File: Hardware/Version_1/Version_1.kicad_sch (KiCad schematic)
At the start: 94 parts, among them IC1 LIFCL-40-7BG256C, IC2 W25R256JVEIQ, IC3 IS46TR16128D-125KBLA2, IC4 TPS62A01DRLR, IC5 TPS62A01DRLR, IC6 TPS62A01DRLR, J1 GPIO, J2 Conn_01x05_Pin, J3 52435-2271, J4 52435-2271, U1 CAT24C256, Y1 AK3ADDF1-156.2500T3

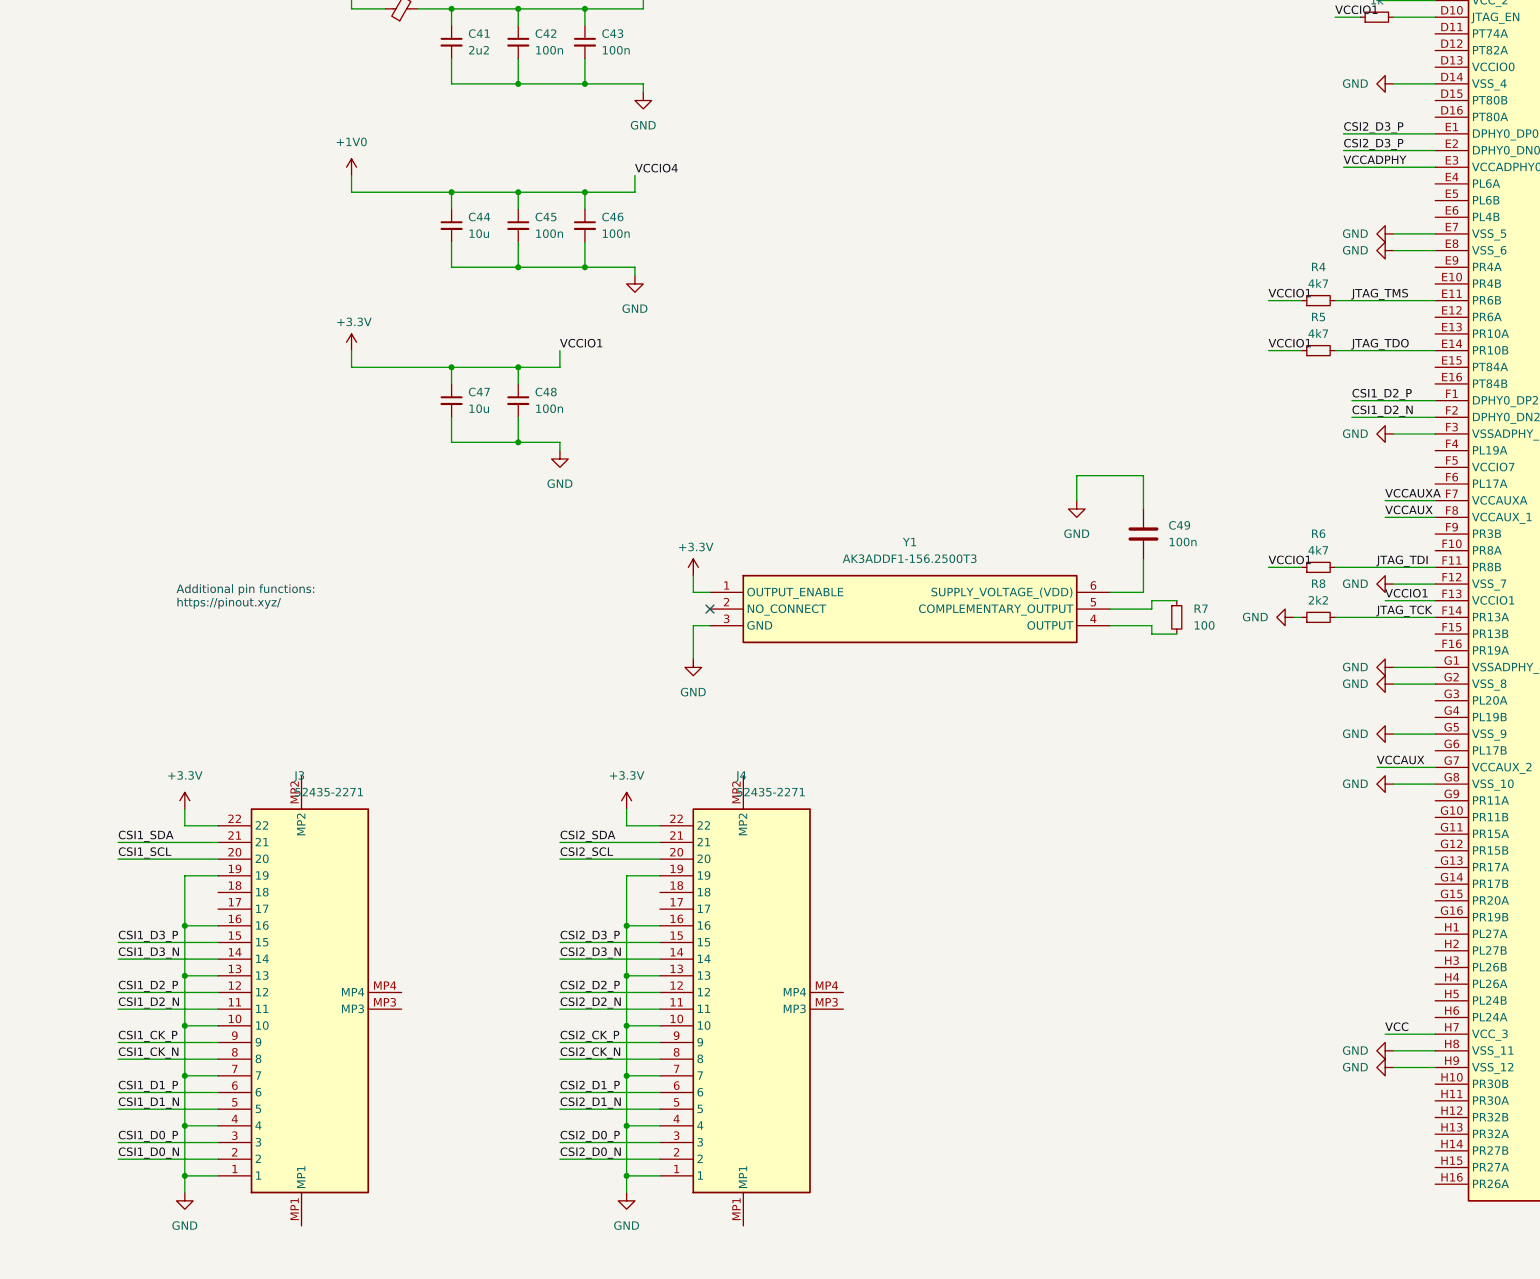
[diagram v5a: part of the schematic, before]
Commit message: mipi routing
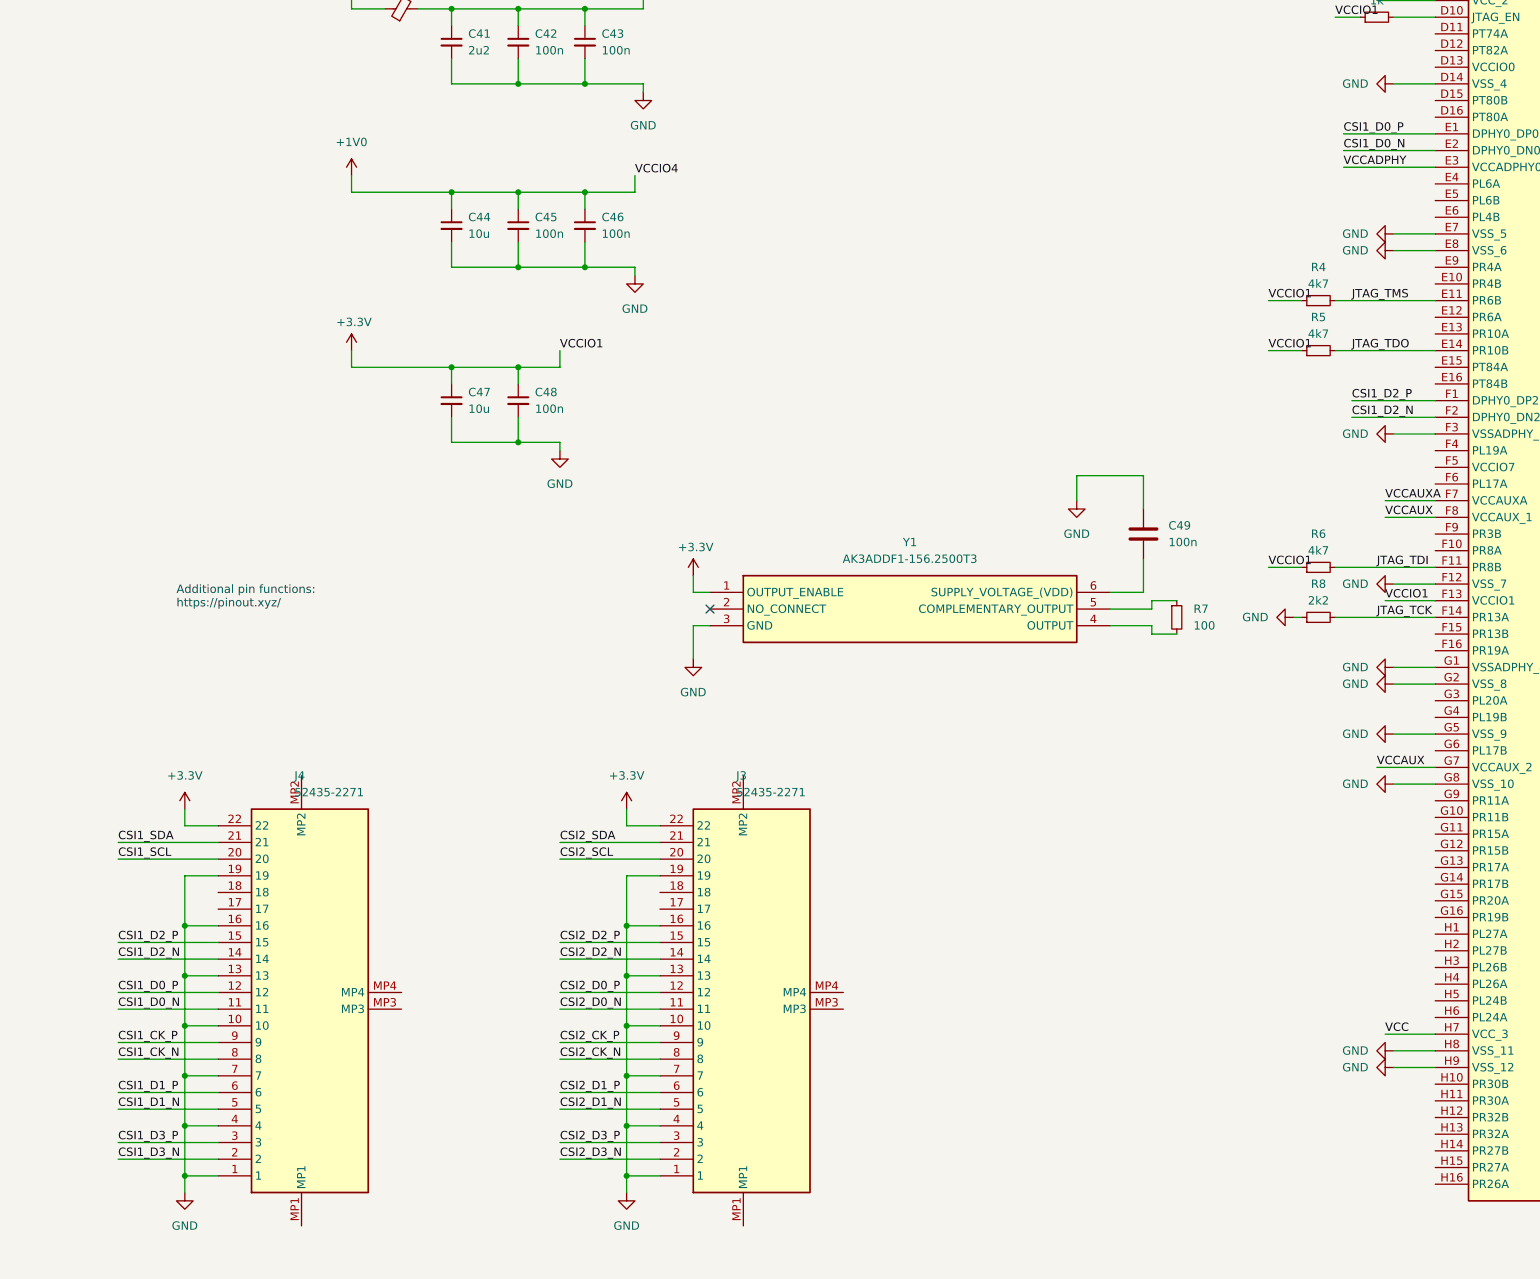
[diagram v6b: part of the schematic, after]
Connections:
- net CSI1_CK_N: now also J4.8; no longer J3.8
- net CSI1_CK_P: now also J4.9; no longer J3.9
- net CSI1_D0_N: now also IC1.E2 (DPHY0_DN0), J4.11; no longer J3.2
- net CSI1_D0_P: now also IC1.E1 (DPHY0_DP0), J4.12; no longer J3.3
- net CSI1_D1_N: now also J4.5; no longer J3.5
- net CSI1_D1_P: now also J4.6; no longer J3.6
- net CSI1_D2_N: now also J4.14; no longer J3.11
- net CSI1_D2_P: now also J4.15; no longer J3.12
- net CSI1_D3_N: now also J4.2; no longer J3.14
- net CSI1_D3_P: now also J4.3; no longer J3.15
- net CSI1_SCL: now also J4.20; no longer J3.20
- net CSI1_SDA: now also J4.21; no longer J3.21
- net CSI2_CK_N: now also J3.8; no longer J4.8
- net CSI2_CK_P: now also J3.9; no longer J4.9
- net CSI2_D0_N: now also J3.11; no longer J4.2
- net CSI2_D0_P: now also J3.12; no longer J4.3
- net CSI2_D1_N: now also J3.5; no longer J4.5
- net CSI2_D1_P: now also J3.6; no longer J4.6
- net CSI2_D2_N: now also J3.14; no longer J4.11
- net CSI2_D2_P: now also J3.15; no longer J4.12
- net CSI2_D3_N: now also J3.2; no longer J4.14
- net CSI2_D3_P: now also J3.3; no longer IC1.E1 (DPHY0_DP0), IC1.E2 (DPHY0_DN0), J4.15
- net CSI2_SCL: now also J3.20; no longer J4.20
- net CSI2_SDA: now also J3.21; no longer J4.21
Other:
- moved on the sheet: J3, J4
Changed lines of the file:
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@@
     (effects (font (size 1.27 1.27)) (justify left bottom))
   )
-  (label "CSI2_D0_P" (at 222.25 367.03 0) (fields_autoplaced)
+  (label "CSI2_D3_P" (at 222.25 367.03 0) (fields_autoplaced)
     (effects (font (size 1.27 1.27)) (justify left bottom))
   )
@@
     (effects (font (size 1.27 1.27)) (justify left bottom))
   )
-  (label "CSI2_D3_N" (at 222.25 339.09 0) (fields_autoplaced)
+  (label "CSI2_D2_N" (at 222.25 339.09 0) (fields_autoplaced)
     (effects (font (size 1.27 1.27)) (justify left bottom))
   )
@@
     (effects (font (size 1.27 1.27)) (justify left bottom))
   )
-  (label "CSI2_D2_N" (at 222.25 346.71 0) (fields_autoplaced)
+  (label "CSI2_D0_N" (at 222.25 346.71 0) (fields_autoplaced)
     (effects (font (size 1.27 1.27)) (justify left bottom))
   )
@@
     (effects (font (size 1.27 1.27)) (justify left bottom))
   )
-  (label "CSI2_D3_P" (at 341.63 213.36 0) (fields_autoplaced)
+  (label "CSI1_D0_P" (at 341.63 213.36 0) (fields_autoplaced)
     (effects (font (size 1.27 1.27)) (justify left bottom))
   )
@@
     (effects (font (size 1.27 1.27)) (justify left bottom))
   )
-  (label "CSI2_D0_N" (at 222.25 369.57 0) (fields_autoplaced)
+  (label "CSI2_D3_N" (at 222.25 369.57 0) (fields_autoplaced)
     (effects (font (size 1.27 1.27)) (justify left bottom))
   )
@@
     (effects (font (size 1.27 1.27)) (justify left bottom))
   )
-  (label "CSI1_D2_P" (at 154.94 344.17 0) (fields_autoplaced)
+  (label "CSI1_D0_P" (at 154.94 344.17 0) (fields_autoplaced)
     (effects (font (size 1.27 1.27)) (justify left bottom))
   )
@@
     (effects (font (size 1.27 1.27)) (justify left bottom))
   )
-  (label "CSI1_D0_N" (at 154.94 369.57 0) (fields_autoplaced)
+  (label "CSI1_D3_N" (at 154.94 369.57 0) (fields_autoplaced)
     (effects (font (size 1.27 1.27)) (justify left bottom))
   )
@@
     (effects (font (size 1.27 1.27)) (justify left bottom))
   )
-  (label "CSI1_D2_N" (at 154.94 346.71 0) (fields_autoplaced)
+  (label "CSI1_D0_N" (at 154.94 346.71 0) (fields_autoplaced)
     (effects (font (size 1.27 1.27)) (justify left bottom))
   )
@@
     (effects (font (size 1.27 1.27)) (justify right bottom))
   )
-  (label "CSI1_D3_P" (at 154.94 336.55 0) (fields_autoplaced)
+  (label "CSI1_D2_P" (at 154.94 336.55 0) (fields_autoplaced)
     (effects (font (size 1.27 1.27)) (justify left bottom))
   )
@@
     (effects (font (size 1.27 1.27)) (justify left bottom))
   )
-  (label "CSI2_D2_P" (at 222.25 344.17 0) (fields_autoplaced)
+  (label "CSI2_D0_P" (at 222.25 344.17 0) (fields_autoplaced)
     (effects (font (size 1.27 1.27)) (justify left bottom))
   )
@@
     (effects (font (size 1.27 1.27)) (justify left bottom))
   )
-  (label "CSI2_D3_P" (at 341.63 215.9 0) (fields_autoplaced)
+  (label "CSI1_D0_N" (at 341.63 215.9 0) (fields_autoplaced)
     (effects (font (size 1.27 1.27)) (justify left bottom))
   )
@@
     (effects (font (size 1.27 1.27)) (justify left bottom))
   )
-  (label "CSI1_D0_P" (at 154.94 367.03 0) (fields_autoplaced)
+  (label "CSI1_D3_P" (at 154.94 367.03 0) (fields_autoplaced)
     (effects (font (size 1.27 1.27)) (justify left bottom))
   )
@@
     (effects (font (size 1.27 1.27)) (justify left bottom))
   )
-  (label "CSI2_D3_P" (at 222.25 336.55 0) (fields_autoplaced)
+  (label "CSI2_D2_P" (at 222.25 336.55 0) (fields_autoplaced)
     (effects (font (size 1.27 1.27)) (justify left bottom))
   )
-  (label "CSI1_D3_N" (at 154.94 339.09 0) (fields_autoplaced)
+  (label "CSI1_D2_N" (at 154.94 339.09 0) (fields_autoplaced)
     (effects (font (size 1.27 1.27)) (justify left bottom))
   )
@@
     )
   )
-  (symbol (lib_id "Component:52435-2271") (at 250.19 379.73 90) (unit 1)
+  (symbol (lib_id "Component:52435-2271") (at 182.88 379.73 90) (unit 1)
     (in_bom yes) (on_board yes) (dnp no) (fields_autoplaced)
-    (property "Reference" "J4" (at 249.1039 311.15 90)
+    (property "Reference" "J4" (at 181.7939 311.15 90)
       (effects (font (size 1.27 1.27)) (justify right))
     )
-    (property "Value" "52435-2271" (at 249.1039 313.69 90)
+    (property "Value" "52435-2271" (at 181.7939 313.69 90)
       (effects (font (size 1.27 1.27)) (justify right))
     )
-    (property "Footprint" "524352271" (at 340.03 314.96 0)
+    (property "Footprint" "524352271" (at 272.72 314.96 0)
       (effects (font (size 1.27 1.27)) (justify left top) hide)
     )
-    (property "Datasheet" "https://www.molex.com/pdm_docs/sd/524352271_sd.pdf" (at 440.03 314.96 0)
+    (property "Datasheet" "https://www.molex.com/pdm_docs/sd/524352271_sd.pdf" (at 372.72 314.96 0)
       (effects (font (size 1.27 1.27)) (justify left top) hide)
     )
-    (property "Height" "2.2" (at 640.03 314.96 0)
+    (property "Height" "2.2" (at 572.72 314.96 0)
       (effects (font (size 1.27 1.27)) (justify left top) hide)
     )
-    (property "Manufacturer_Name" "Molex" (at 740.03 314.96 0)
+    (property "Manufacturer_Name" "Molex" (at 672.72 314.96 0)
       (effects (font (size 1.27 1.27)) (justify left top) hide)
     )
-    (property "Manufacturer_Part_Number" "52435-2271" (at 840.03 314.96 0)
+    (property "Manufacturer_Part_Number" "52435-2271" (at 772.72 314.96 0)
       (effects (font (size 1.27 1.27)) (justify left top) hide)
     )
-    (property "Mouser Part Number" "538-52435-2271" (at 940.03 314.96 0)
+    (property "Mouser Part Number" "538-52435-2271" (at 872.72 314.96 0)
       (effects (font (size 1.27 1.27)) (justify left top) hide)
     )
-    (property "Mouser Price/Stock" "https://www.mouser.co.uk/ProductDetail/Molex/52435-2271?qs=R7%2FZKp6KZ2YF65bXSszUKA%3D%3D" (at 1040.03 314.96 0)
+    (property "Mouser Price/Stock" "https://www.mouser.co.uk/ProductDetail/Molex/52435-2271?qs=R7%2FZKp6KZ2YF65bXSszUKA%3D%3D" (at 972.72 314.96 0)
       (effects (font (size 1.27 1.27)) (justify left top) hide)
     )
-    (property "Arrow Part Number" "" (at 1140.03 314.96 0)
+    (property "Arrow Part Number" "" (at 1072.72 314.96 0)
       (effects (font (size 1.27 1.27)) (justify left top) hide)
     )
-    (property "Arrow Price/Stock" "" (at 1240.03 314.96 0)
+    (property "Arrow Price/Stock" "" (at 1172.72 314.96 0)
       (effects (font (size 1.27 1.27)) (justify left top) hide)
     )
@@
     )
   )
-  (symbol (lib_id "Component:52435-2271") (at 182.88 379.73 90) (unit 1)
+  (symbol (lib_id "Component:52435-2271") (at 250.19 379.73 90) (unit 1)
     (in_bom yes) (on_board yes) (dnp no) (fields_autoplaced)
-    (property "Reference" "J3" (at 181.7939 311.15 90)
+    (property "Reference" "J3" (at 249.1039 311.15 90)
       (effects (font (size 1.27 1.27)) (justify right))
     )
-    (property "Value" "52435-2271" (at 181.7939 313.69 90)
+    (property "Value" "52435-2271" (at 249.1039 313.69 90)
       (effects (font (size 1.27 1.27)) (justify right))
     )
-    (property "Footprint" "524352271" (at 272.72 314.96 0)
+    (property "Footprint" "524352271" (at 340.03 314.96 0)
       (effects (font (size 1.27 1.27)) (justify left top) hide)
     )
-    (property "Datasheet" "https://www.molex.com/pdm_docs/sd/524352271_sd.pdf" (at 372.72 314.96 0)
+    (property "Datasheet" "https://www.molex.com/pdm_docs/sd/524352271_sd.pdf" (at 440.03 314.96 0)
       (effects (font (size 1.27 1.27)) (justify left top) hide)
     )
-    (property "Height" "2.2" (at 572.72 314.96 0)
+    (property "Height" "2.2" (at 640.03 314.96 0)
       (effects (font (size 1.27 1.27)) (justify left top) hide)
     )
-    (property "Manufacturer_Name" "Molex" (at 672.72 314.96 0)
+    (property "Manufacturer_Name" "Molex" (at 740.03 314.96 0)
       (effects (font (size 1.27 1.27)) (justify left top) hide)
     )
-    (property "Manufacturer_Part_Number" "52435-2271" (at 772.72 314.96 0)
+    (property "Manufacturer_Part_Number" "52435-2271" (at 840.03 314.96 0)
       (effects (font (size 1.27 1.27)) (justify left top) hide)
     )
-    (property "Mouser Part Number" "538-52435-2271" (at 872.72 314.96 0)
+    (property "Mouser Part Number" "538-52435-2271" (at 940.03 314.96 0)
       (effects (font (size 1.27 1.27)) (justify left top) hide)
     )
-    (property "Mouser Price/Stock" "https://www.mouser.co.uk/ProductDetail/Molex/52435-2271?qs=R7%2FZKp6KZ2YF65bXSszUKA%3D%3D" (at 972.72 314.96 0)
+    (property "Mouser Price/Stock" "https://www.mouser.co.uk/ProductDetail/Molex/52435-2271?qs=R7%2FZKp6KZ2YF65bXSszUKA%3D%3D" (at 1040.03 314.96 0)
       (effects (font (size 1.27 1.27)) (justify left top) hide)
     )
-    (property "Arrow Part Number" "" (at 1072.72 314.96 0)
+    (property "Arrow Part Number" "" (at 1140.03 314.96 0)
       (effects (font (size 1.27 1.27)) (justify left top) hide)
     )
-    (property "Arrow Price/Stock" "" (at 1172.72 314.96 0)
+    (property "Arrow Price/Stock" "" (at 1240.03 314.96 0)
       (effects (font (size 1.27 1.27)) (justify left top) hide)
     )

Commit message: Added i2c and flash chip
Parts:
- removed J1: GPIO, Connector_PinSocket_2.54mm:PinSocket_2x20_P2.54mm_Vertical, symbol Connector_Generic:Conn_02x20_Odd_Even
- added DONE1, INITN1: TestPoint, TestPoint:TestPoint_Pad_D1.0mm, symbol Connector:TestPoint
- added J6: GPIO, Connector_PinSocket_2.54mm:PinSocket_2x20_P2.54mm_Vertical, symbol Connector_Generic:Conn_02x20_Odd_Even
- added R18: 1k0, Resistor_SMD:R_0603_1608Metric, symbol Device:R_Small
- added R19, R20: 4k7, Resistor_SMD:R_0603_1608Metric, symbol Device:R_Small
- added R21, R22: 10k0, Resistor_SMD:R_0402_1005Metric, symbol Device:R_Small
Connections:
- net +3.3V: now also R19.1, R20.1
- net +3V3: now also C49.1, Y1.6 (SUPPLY_VOLTAGE_(VDD)), J6.1 (+3V3), J6.17 (+3V3)
- net +5V: now also J6.2 (+5V), J6.4 (+5V)
- net CSI1_SCL: now also IC1.G13 (PR17A)
- net CSI1_SDA: now also IC1.G14 (PR17B)
- net CSI2_SCL: now also IC1.G16 (PR19B)
- net CSI2_SDA: now also IC1.F16 (PR19A)
- net GND: now also C49.2, J6.14 (GND), J6.20 (GND), J6.25 (GND), J6.30 (GND), J6.34 (GND), J6.39 (GND), J6.6 (GND), J6.9 (GND), R18.2, R22.2; no longer C49.1
- net GPIO10/SPI0.MOSI: now also J6.19 (GPIO10/SPI0.MOSI)
- net GPIO11/SPI0.SCLK: now also J6.23 (GPIO11/SPI0.SCLK)
- net GPIO12/PWM0: now also J6.32 (GPIO12/PWM0)
- net GPIO13/PWM1: now also J6.33 (GPIO13/PWM1)
- net GPIO14/TXD0: now also J6.8 (GPIO14/TXD0)
- net GPIO15/RXD0: now also J6.10 (GPIO15/RXD0)
- net GPIO16: now also J6.36 (GPIO16)
- net GPIO17: now also J6.11 (GPIO17)
- net GPIO18/PCM.CLK: now also J6.12 (GPIO18/PCM.CLK)
- net GPIO19/PCM.FS: now also J6.35 (GPIO19/PCM.FS)
- net GPIO20/PCM.DIN: now also J6.38 (GPIO20/PCM.DIN)
- net GPIO21/PCM.DOUT: now also J6.40 (GPIO21/PCM.DOUT)
- net GPIO22: now also J6.15 (GPIO22)
- net GPIO23: now also J6.16 (GPIO23)
- net GPIO24: now also J6.18 (GPIO24)
- net GPIO25: now also J6.22 (GPIO25)
- net GPIO26: now also J6.37 (GPIO26)
- net GPIO27: now also J6.13 (GPIO27)
- net GPIO5: now also J6.29 (GPIO5)
- net GPIO6: now also J6.31 (GPIO6)
- net GPIO7/SPI0.CE1: now also J6.26 (GPIO7/SPI0.CE1)
- net GPIO8/SPI0.CE0: now also J6.24 (GPIO8/SPI0.CE0)
- net GPIO9/SPI0.MISO: now also J6.21 (GPIO9/SPI0.MISO)
- net ID_SCL: now also J6.28 (ID_SCL)
- net ID_SDA: now also J6.27 (ID_SDA)
- net VCCDRAM: now also IC3.T2 (RESET#), R21.1
- net DONE: now reaches IC1.B16 (PT76B)
- net DONE: now also DONE1.1
- net PROGRAMN: now reaches IC1.C12 (PT74B)
- net PROGRAMN: now also J6.7 (GPIO4/GPCLK0), R20.2
- net MD0: now reaches IC1.C14 (PT78B)
- net MD0: now also IC2.5 (IO0)
- net MCSN: now reaches IC1.C15 (PT78A)
- net MCSN: now also IC2.1 (~{CS}), R19.2
- net MCLK: now reaches IC1.C16 (PT76A)
- net MCLK: now also IC2.6 (CLK), R18.1
- net INITN: now reaches IC1.D11 (PT74A)
- net INITN: now also INITN1.1
- net MD3: now reaches IC1.D12 (PT82A)
- net MD3: now also IC2.7 (IO3)
- net MD2: now reaches IC1.D15 (PT80B)
- net MD2: now also IC2.3 (IO2)
- net MD1: now reaches IC1.D16 (PT80A)
- net MD1: now also IC2.2 (IO1)
- net SLAVE_I2C_SCL: now reaches IC1.G10 (PR11B)
- net SLAVE_I2C_SCL: now also J6.5 (GPIO3/SCL1)
- net SLAVE_I2C_SDA: now reaches IC1.G9 (PR11A)
- net SLAVE_I2C_SDA: now also J6.3 (GPIO2/SDA1)
- net REFCLK_N: now reaches IC1.M4 (PB6B)
- net REFCLK_N: now also R7.1, Y1.5 (COMPLEMENTARY_OUTPUT)
- net REFCLK_P: now reaches IC1.N4 (PB6A)
- net REFCLK_P: now also R7.2, Y1.4 (OUTPUT)
- net DML: now reaches IC1.R8 (PB42A)
- net DML: now also IC3.E7 (DML)
- net DMU: now reaches IC1.T4 (PB20B)
- net DMU: now also IC3.D3 (DMU)
- net DRAM_VREF: now reaches IC3.H1 (VREFDQ)
- net DRAM_VREF: now also IC3.M8 (VREFCA), R21.2, R22.1
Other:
- moved on the sheet: C18, C49

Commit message: Layout for JTAG
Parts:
- added J1: Conn_01x02_Pin, Connector_PinHeader_2.54mm:PinHeader_1x02_P2.54mm_Vertical, symbol Connector:Conn_01x02_Pin
- added JP3: Jumper_3_Bridged12, Connector_PinHeader_2.54mm:PinHeader_1x03_P2.54mm_Vertical, symbol Jumper:Jumper_3_Bridged12
- added R23: 4k7, Resistor_SMD:R_0603_1608Metric, symbol Device:R_Small
- R3: footprint Resistor_SMD:R_0603_1608Metric -> Resistor_SMD:R_0402_1005Metric
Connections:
- net +3.3V is gone; now on net +3V3: C18.1, IC2.8 (VCC), J3.22, J4.22, R19.1, R20.1
- net +3V3: now also R23.2; no longer R3.1
- net A2: no longer IC1.L10 (PB80B)
- net GND: now also J1.1 (Pin_1), JP3.3 (B)
- net JTAG_TCK: now also J2.3 (Pin_3); no longer J2.4 (Pin_4)
- net JTAG_TDI: now also J2.4 (Pin_4); no longer J2.1 (Pin_1)
- net JTAG_TMS: now also J2.5 (Pin_5); no longer J2.3 (Pin_3)
- net PROGRAMN: now also JP3.2 (C); no longer J6.7 (GPIO4/GPCLK0), R20.2
- new net: J2.1 (Pin_1), R23.1
- new net: JP3.1 (A), R20.2
- new net JTAG_EN: J1.2 (Pin_2), R3.1
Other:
- moved on the sheet: INITN1, R3
